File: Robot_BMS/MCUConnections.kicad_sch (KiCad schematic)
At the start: 0 parts

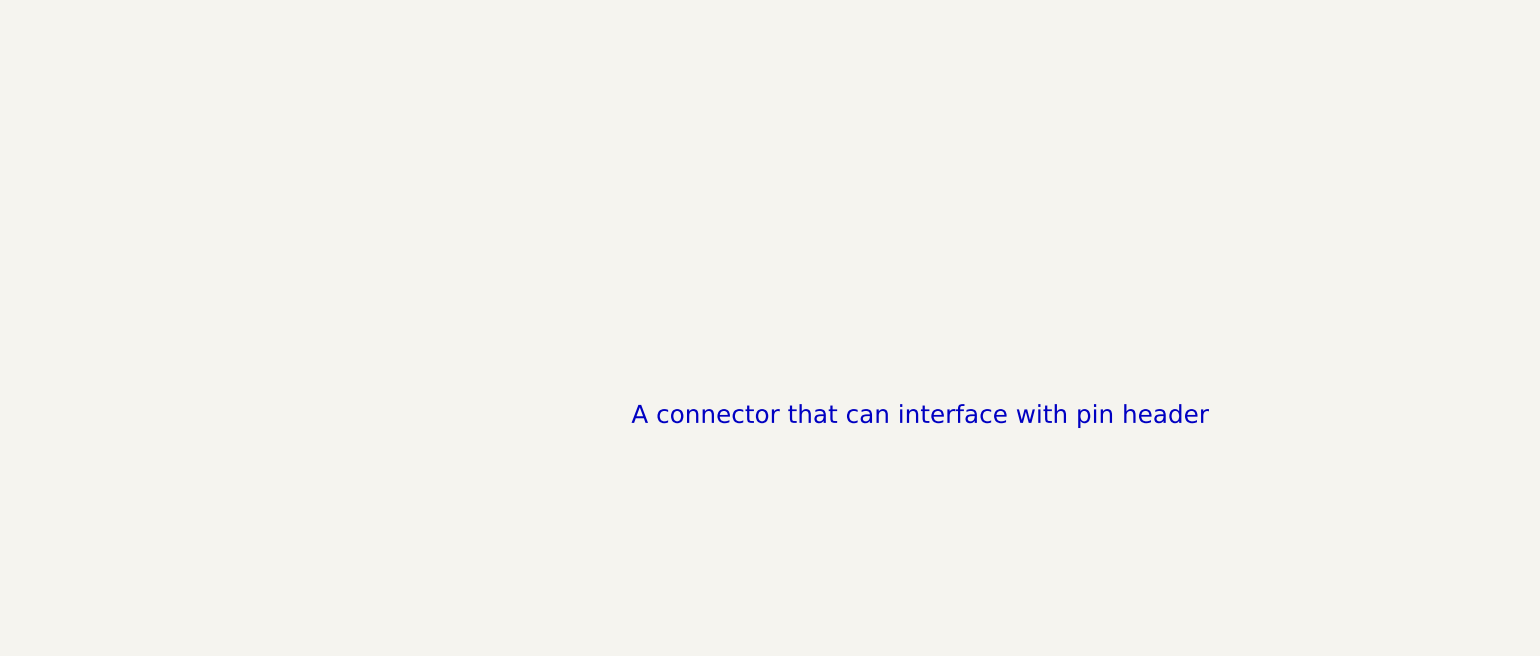
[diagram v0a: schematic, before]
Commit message: DC power supply added via dc Barrel jack
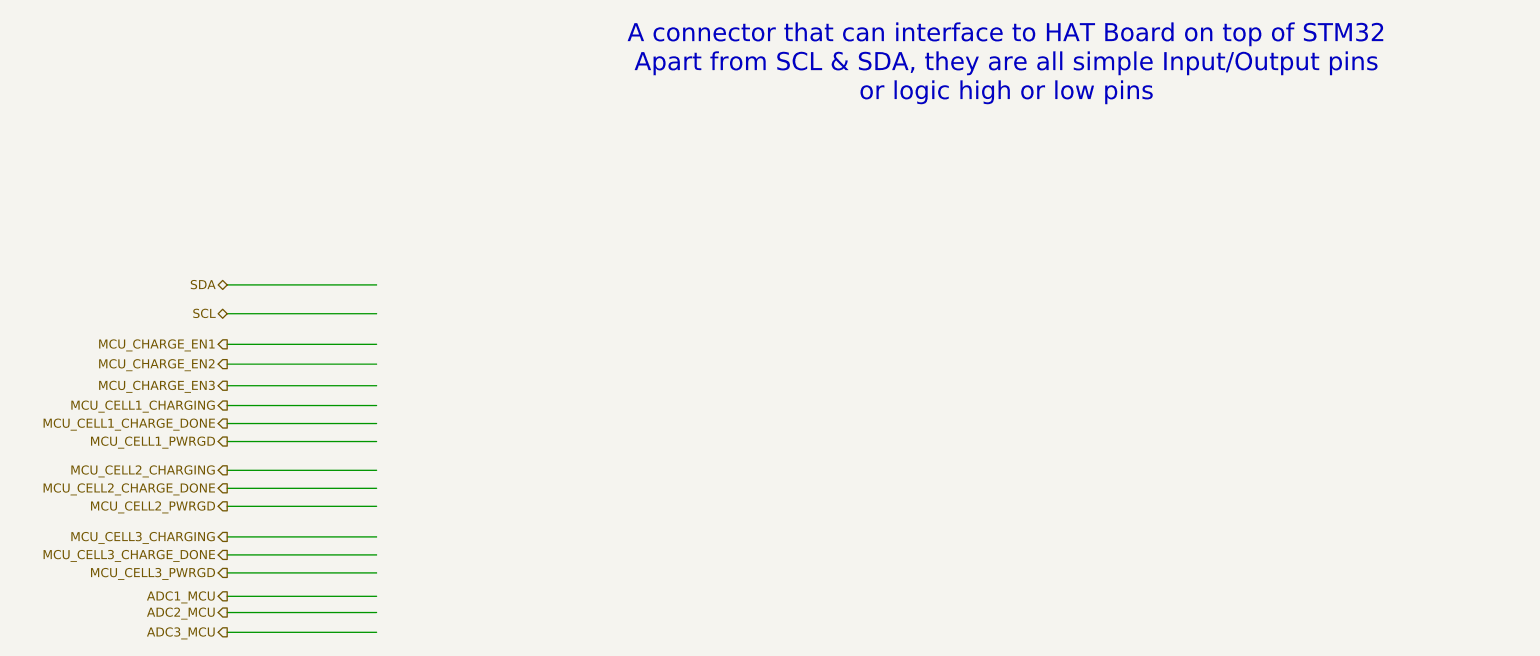
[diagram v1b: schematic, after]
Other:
- note added: "A connector that can interface to HAT Board on top of STM32 Apart from SCL & SDA, they are all simple Input/Output pins or logic high or low pins"
- note removed: "A connector that can interface with pin header"

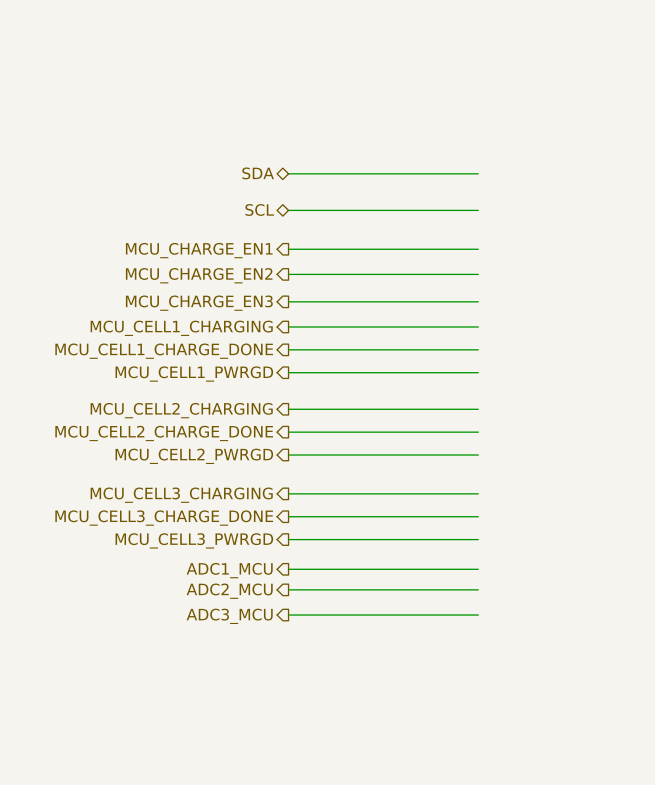
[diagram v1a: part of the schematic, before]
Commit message: System drawing down on top schematic, will start inputting footprints
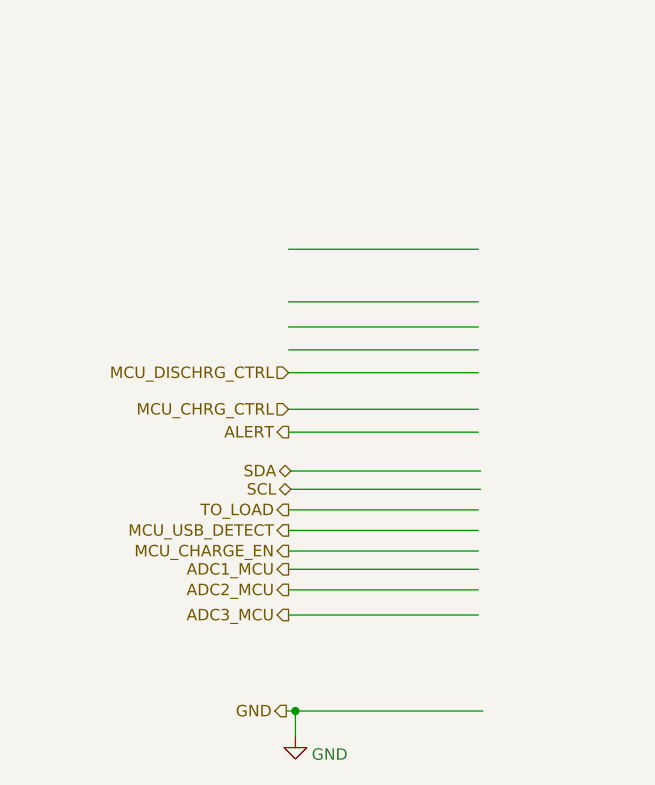
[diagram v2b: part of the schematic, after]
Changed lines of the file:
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@@
 		(date "2025-03-13")
 	)
+	(junction
+		(at 82.042 129.286)
+		(diameter 0)
+		(color 0 0 0 0)
+	)
 	(wire
 		(pts
@@
 	(wire
 		(pts
-			(xy 81.28 107.696) (xy 102.362 107.696)
-		)
-		(stroke
-			(width 0)
-			(type default)
-		)
-	)
-	(wire
-		(pts
 			(xy 81.28 83.82) (xy 102.362 83.82)
 		)
@@
 	(wire
 		(pts
-			(xy 81.28 105.156) (xy 102.362 105.156)
+			(xy 81.28 111.506) (xy 102.362 111.506)
 		)
 		(stroke
@@
 	(wire
 		(pts
-			(xy 81.28 110.236) (xy 102.362 110.236)
+			(xy 82.042 129.286) (xy 102.87 129.286)
 		)
 		(stroke
@@
 	(wire
 		(pts
-			(xy 81.28 69.596) (xy 102.362 69.596)
+			(xy 81.534 102.616) (xy 102.616 102.616)
+		)
+		(stroke
+			(width 0)
+			(type default)
+		)
+	)
+	(wire
+		(pts
+			(xy 81.026 129.286) (xy 82.042 129.286)
 		)
 		(stroke
@@
 	(wire
 		(pts
-			(xy 81.28 100.838) (xy 102.362 100.838)
+			(xy 81.28 109.22) (xy 102.362 109.22)
 		)
 		(stroke
@@
 	(wire
 		(pts
-			(xy 81.28 80.772) (xy 102.362 80.772)
-		)
-		(stroke
-			(width 0)
-			(type default)
-		)
-	)
-	(wire
-		(pts
-			(xy 81.28 73.66) (xy 102.362 73.66)
+			(xy 81.28 106.934) (xy 102.362 106.934)
+		)
+		(stroke
+			(width 0)
+			(type default)
+		)
+	)
+	(wire
+		(pts
+			(xy 81.534 104.648) (xy 102.616 104.648)
+		)
+		(stroke
+			(width 0)
+			(type default)
+		)
+	)
+	(wire
+		(pts
+			(xy 82.042 129.286) (xy 82.042 132.08)
 		)
 		(stroke
@@
 		)
 	)
-	(hierarchical_label "MCU_CELL1_PWRGD"
-		(shape output)
-		(at 81.28 91.694 180)
-		(effects
-			(font
-				(size 1.27 1.27)
-			)
-			(justify right)
-		)
-	)
-	(hierarchical_label "MCU_CELL3_CHARGING"
-		(shape output)
-		(at 81.28 105.156 180)
+	(hierarchical_label "TO_LOAD"
+		(shape output)
+		(at 81.28 106.934 180)
+		(effects
+			(font
+				(size 1.27 1.27)
+			)
+			(justify right)
+		)
+	)
+	(hierarchical_label "MCU_CHRG_CTRL"
+		(shape input)
+		(at 81.28 95.758 180)
 		(effects
 			(font
@@
 	(hierarchical_label "SCL"
 		(shape bidirectional)
-		(at 81.28 73.66 180)
+		(at 81.534 104.648 180)
 		(effects
 			(font
@@
 		)
 	)
-	(hierarchical_label "MCU_CELL2_CHARGING"
-		(shape output)
-		(at 81.28 95.758 180)
-		(effects
-			(font
-				(size 1.27 1.27)
-			)
-			(justify right)
-		)
-	)
-	(hierarchical_label "MCU_CELL3_CHARGE_DONE"
-		(shape output)
-		(at 81.28 107.696 180)
-		(effects
-			(font
-				(size 1.27 1.27)
-			)
-			(justify right)
-		)
-	)
-	(hierarchical_label "MCU_CELL2_CHARGE_DONE"
+	(hierarchical_label "MCU_DISCHRG_CTRL"
+		(shape input)
+		(at 81.28 91.694 180)
+		(effects
+			(font
+				(size 1.27 1.27)
+			)
+			(justify right)
+		)
+	)
+	(hierarchical_label "MCU_CHARGE_EN"
+		(shape output)
+		(at 81.28 111.506 180)
+		(effects
+			(font
+				(size 1.27 1.27)
+			)
+			(justify right)
+		)
+	)
+	(hierarchical_label "ADC2_MCU"
+		(shape output)
+		(at 81.28 115.824 180)
+		(effects
+			(font
+				(size 1.27 1.27)
+			)
+			(justify right)
+		)
+	)
+	(hierarchical_label "GND"
+		(shape output)
+		(at 81.026 129.286 180)
+		(effects
+			(font
+				(size 1.27 1.27)
+			)
+			(justify right)
+		)
+	)
+	(hierarchical_label "ALERT"
 		(shape output)
 		(at 81.28 98.298 180)
-		(effects
-			(font
-				(size 1.27 1.27)
-			)
-			(justify right)
-		)
-	)
-	(hierarchical_label "MCU_CHARGE_EN2"
-		(shape output)
-		(at 81.28 80.772 180)
-		(effects
-			(font
-				(size 1.27 1.27)
-			)
-			(justify right)
-		)
-	)
-	(hierarchical_label "MCU_CELL1_CHARGE_DONE"
-		(shape output)
-		(at 81.28 89.154 180)
-		(effects
-			(font
-				(size 1.27 1.27)
-			)
-			(justify right)
-		)
-	)
-	(hierarchical_label "MCU_CELL3_PWRGD"
-		(shape output)
-		(at 81.28 110.236 180)
-		(effects
-			(font
-				(size 1.27 1.27)
-			)
-			(justify right)
-		)
-	)
-	(hierarchical_label "MCU_CHARGE_EN3"
-		(shape output)
-		(at 81.28 83.82 180)
-		(effects
-			(font
-				(size 1.27 1.27)
-			)
-			(justify right)
-		)
-	)
-	(hierarchical_label "MCU_CELL2_PWRGD"
-		(shape output)
-		(at 81.28 100.838 180)
-		(effects
-			(font
-				(size 1.27 1.27)
-			)
-			(justify right)
-		)
-	)
-	(hierarchical_label "ADC2_MCU"
-		(shape output)
-		(at 81.28 115.824 180)
 		(effects
 			(font
@@
 	(hierarchical_label "SDA"
 		(shape bidirectional)
-		(at 81.28 69.596 180)
-		(effects
-			(font
-				(size 1.27 1.27)
-			)
-			(justify right)
-		)
-	)
-	(hierarchical_label "MCU_CELL1_CHARGING"
-		(shape output)
-		(at 81.28 86.614 180)
-		(effects
-			(font
-				(size 1.27 1.27)
-			)
-			(justify right)
-		)
-	)
-	(hierarchical_label "MCU_CHARGE_EN1"
-		(shape output)
-		(at 81.28 77.978 180)
-		(effects
-			(font
-				(size 1.27 1.27)
-			)
-			(justify right)
-		)
-	)
+		(at 81.534 102.616 180)
+		(effects
+			(font
+				(size 1.27 1.27)
+			)
+			(justify right)
+		)
+	)
+	(hierarchical_label "MCU_USB_DETECT"
+		(shape output)
+		(at 81.28 109.22 180)
+		(effects
+			(font
+				(size 1.27 1.27)
+			)
+			(justify right)
+		)
+	)
+	(symbol
+		(lib_id "power:GND")
+		(at 82.042 132.08 0)
+		(mirror y)
+		(unit 1)
+		(exclude_from_sim no)
+		(in_bom yes)
+		(on_board yes)
+		(dnp no)
+		(property "Reference" "#PWR018"
+			(at 82.042 138.43 0)
+			(effects
+				(font
+					(size 1.27 1.27)
+				)
+				(hide yes)
+			)
+		)
+		(property "Value" "GND"
+			(at 85.852 134.112 0)
+			(effects
+				(font
+					(size 1.27 1.27)
+				)
+			)
+		)
+		(property "Footprint" ""
+			(at 82.042 132.08 0)
+			(effects
+				(font
+					(size 1.27 1.27)
+				)
+				(hide yes)
+			)
+		)
+		(property "Datasheet" ""
+			(at 82.042 132.08 0)
+			(effects
+				(font
+					(size 1.27 1.27)
+				)
+				(hide yes)
+			)
+		)
+		(property "Description" "Power symbol creates a global label with name \"GND\" , ground"
+			(at 82.042 132.08 0)
+			(effects
+				(font
+					(size 1.27 1.27)
+				)
+				(hide yes)
+			)
+		)
+		(pin "1"
+		)
+		(instances
+			(project "Robot_BMS"
+				(path "/72551b1c-3d40-4199-8911-e5b015f4abec/f21d0d80-f932-4fe7-82f0-3490cb74f2de"
+					(reference "#PWR018")
+					(unit 1)
+				)
+			)
+		)
+	)

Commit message: adding footprints and actual passive components
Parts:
- added J2: Conn_01x14_Pin, Connector_PinHeader_2.54mm:PinHeader_1x14_P2.54mm_Vertical, symbol Connector:Conn_01x14_Pin
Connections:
- net ADC1_MCU: now also J2.5 (Pin_5)
- net ADC2_MCU: now also J2.4 (Pin_4)
- net ADC3_MCU: now also J2.3 (Pin_3)
- net ALERT: now also J2.11 (Pin_11)
- net GND: now also J2.2 (Pin_2)
- net MCU_CHARGE_EN: now also J2.6 (Pin_6)
- net MCU_CHRG_CTRL: now also J2.12 (Pin_12)
- net MCU_DISCHRG_CTRL: now also J2.13 (Pin_13)
- net MCU_USB_DETECT: now also J2.7 (Pin_7)
- net SCL: now also J2.9 (Pin_9)
- net SDA: now also J2.10 (Pin_10)
- net TO_LOAD: now also J2.8 (Pin_8)
- new net 3V3: J2.14 (Pin_14)
- no-connect marks 0 -> 1
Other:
- note added: "All standard Passive componenets are 0603 imperial"

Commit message: BOM done, with total price £40
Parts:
- J2: Manufacturer_Part_Number (none) -> 61301411121; Price (none) -> 0.67
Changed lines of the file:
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@@
 			)
 		)
-		(property "Datasheet" "~"
+		(property "Datasheet" "https://www.digikey.co.uk/en/products/detail/w-rth-elektronik/61301411121/4846849?gclsrc=aw.ds&&utm_adgroup=&utm_source=google&utm_medium=cpc&utm_campaign=PMax%20Shopping_Product_New%20Customer%20Acquisition&utm_term=&productid=4846849&utm_content=&utm_id=go_cmp-19905262708_adg-_ad-__dev-c_ext-_prd-4846849_sig-Cj0KCQjw1um-BhDtARIsABjU5x5IZchPm1Re5jb8lZ6dm-_WGVxZLQDpy4bDA0Enw1KwuXt_1ODZSgUaAiIqEALw_wcB&gad_source=1&gclid=Cj0KCQjw1um-BhDtARIsABjU5x5IZchPm1Re5jb8lZ6dm-_WGVxZLQDpy4bDA0Enw1KwuXt_1ODZSgUaAiIqEALw_wcB&gclsrc=aw.ds"
 			(at 112.268 105.918 0)
 			(effects
@@
 			(at 112.268 105.918 0)
 			(effects
+				(font
+					(size 1.27 1.27)
+				)
+				(hide yes)
+			)
+		)
+		(property "Price" "0.67"
+			(at 112.268 105.918 0)
+			(effects
+				(font
+					(size 1.27 1.27)
+				)
+				(hide yes)
+			)
+		)
+		(property "Manufacturer_Part_Number" "61301411121"
+			(at 112.268 105.918 0)
+			(effects

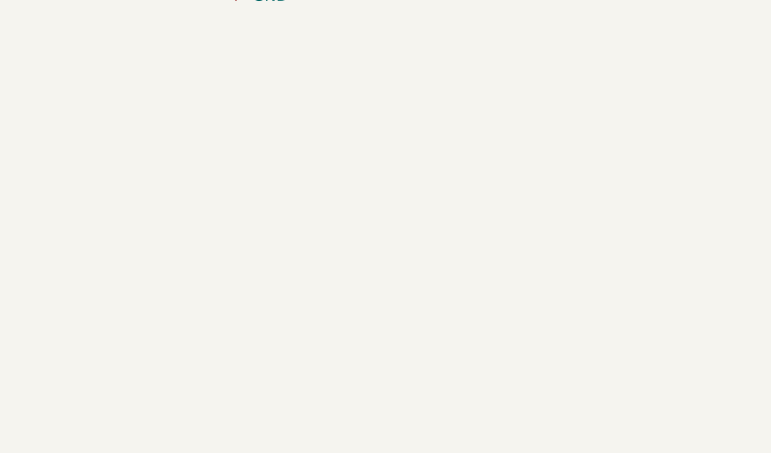
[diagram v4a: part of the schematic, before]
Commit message: switching usb c pd chip to ap33772 due to better support online
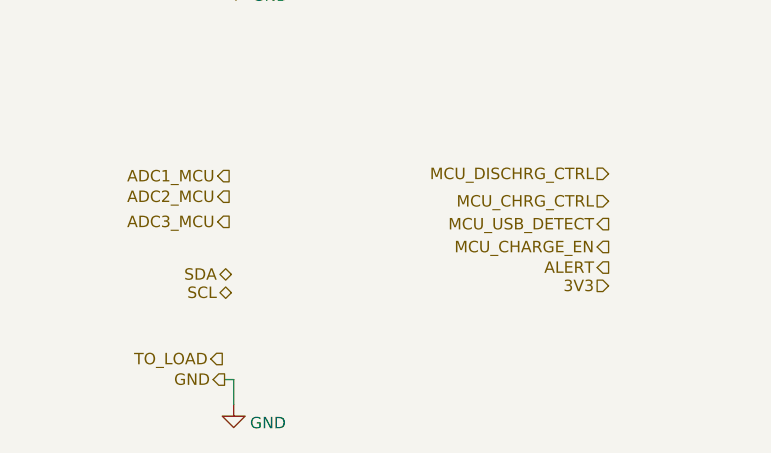
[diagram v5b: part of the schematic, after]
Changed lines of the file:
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@@
+	(wire
+		(pts
+			(xy 81.788 176.784) (xy 81.788 179.578)
+		)
+		(stroke
+			(width 0)
+			(type default)
+		)
+	)
 	(wire
 		(pts
@@
 		(pts
 			(xy 80.772 100.584) (xy 102.87 100.584)
+		)
+		(stroke
+			(width 0)
+			(type default)
+		)
+	)
+	(wire
+		(pts
+			(xy 80.772 176.784) (xy 81.788 176.784)
 		)
 		(stroke
@@
 		)
 	)
+	(hierarchical_label "ADC1_MCU"
+		(shape output)
+		(at 81.28 154.178 180)
+		(effects
+			(font
+				(size 1.27 1.27)
+			)
+			(justify right)
+		)
+	)
+	(hierarchical_label "MCU_USB_DETECT"
+		(shape output)
+		(at 123.444 159.512 180)
+		(effects
+			(font
+				(size 1.27 1.27)
+			)
+			(justify right)
+		)
+	)
 	(hierarchical_label "TO_LOAD"
 		(shape output)
@@
 		)
 	)
+	(hierarchical_label "MCU_CHARGE_EN"
+		(shape output)
+		(at 123.444 162.052 180)
+		(effects
+			(font
+				(size 1.27 1.27)
+			)
+			(justify right)
+		)
+	)
 	(hierarchical_label "SCL"
 		(shape bidirectional)
@@
 		)
 	)
+	(hierarchical_label "TO_LOAD"
+		(shape output)
+		(at 80.518 174.498 180)
+		(effects
+			(font
+				(size 1.27 1.27)
+			)
+			(justify right)
+		)
+	)
 	(hierarchical_label "ADC3_MCU"
 		(shape output)
 		(at 82.042 116.84 180)
+		(effects
+			(font
+				(size 1.27 1.27)
+			)
+			(justify right)
+		)
+	)
+	(hierarchical_label "MCU_DISCHRG_CTRL"
+		(shape input)
+		(at 123.444 153.924 180)
 		(effects
 			(font
@@
 		)
 	)
+	(hierarchical_label "MCU_CHRG_CTRL"
+		(shape input)
+		(at 123.444 156.972 180)
+		(effects
+			(font
+				(size 1.27 1.27)
+			)
+			(justify right)
+		)
+	)
+	(hierarchical_label "3V3"
+		(shape input)
+		(at 123.444 166.37 180)
+		(effects
+			(font
+				(size 1.27 1.27)
+			)
+			(justify right)
+		)
+	)
+	(hierarchical_label "SDA"
+		(shape bidirectional)
+		(at 81.534 165.1 180)
+		(effects
+			(font
+				(size 1.27 1.27)
+			)
+			(justify right)
+		)
+	)
+	(hierarchical_label "ALERT"
+		(shape output)
+		(at 123.444 164.338 180)
+		(effects
+			(font
+				(size 1.27 1.27)
+			)
+			(justify right)
+		)
+	)
+	(hierarchical_label "ADC3_MCU"
+		(shape output)
+		(at 81.28 159.258 180)
+		(effects
+			(font
+				(size 1.27 1.27)
+			)
+			(justify right)
+		)
+	)
 	(hierarchical_label "ADC2_MCU"
 		(shape output)
 		(at 82.042 114.046 180)
+		(effects
+			(font
+				(size 1.27 1.27)
+			)
+			(justify right)
+		)
+	)
+	(hierarchical_label "ADC2_MCU"
+		(shape output)
+		(at 81.28 156.464 180)
 		(effects
 			(font
@@
 		)
 	)
+	(hierarchical_label "GND"
+		(shape output)
+		(at 80.772 176.784 180)
+		(effects
+			(font
+				(size 1.27 1.27)
+			)
+			(justify right)
+		)
+	)
 	(hierarchical_label "MCU_USB_DETECT"
 		(shape output)
 		(at 81.534 106.934 180)
+		(effects
+			(font
+				(size 1.27 1.27)
+			)
+			(justify right)
+		)
+	)
+	(hierarchical_label "SCL"
+		(shape bidirectional)
+		(at 81.534 167.132 180)
 		(effects
 			(font
@@
 		)
 	)
+	(symbol
+		(lib_id "power:GND")
+		(at 81.788 179.578 0)
+		(mirror y)
+		(unit 1)
+		(exclude_from_sim no)
+		(in_bom yes)
+		(on_board yes)
+		(dnp no)
+		(property "Reference" "#PWR039"
+			(at 81.788 185.928 0)
+			(effects
+				(font
+					(size 1.27 1.27)
+				)
+				(hide yes)
+			)
+		)
+		(property "Value" "GND"
+			(at 85.598 181.61 0)
+			(effects
+				(font
+					(size 1.27 1.27)
+				)
+			)
+		)
+		(property "Footprint" ""
+			(at 81.788 179.578 0)
+			(effects
+				(font
+					(size 1.27 1.27)
+				)
+				(hide yes)
+			)
+		)
+		(property "Datasheet" ""
+			(at 81.788 179.578 0)
+			(effects
+				(font
+					(size 1.27 1.27)
+				)
+				(hide yes)
+			)
+		)
+		(property "Description" "Power symbol creates a global label with name \"GND\" , ground"
+			(at 81.788 179.578 0)
+			(effects
+				(font
+					(size 1.27 1.27)
+				)
+				(hide yes)
+			)
+		)
+		(pin "1"
+		)
+		(instances
+			(project "Robot_BMS"
+				(path "/72551b1c-3d40-4199-8911-e5b015f4abec/f21d0d80-f932-4fe7-82f0-3490cb74f2de"
+					(reference "#PWR039")
+					(unit 1)
+				)
+			)
+		)
+	)
